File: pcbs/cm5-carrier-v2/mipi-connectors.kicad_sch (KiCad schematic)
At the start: 6 parts, among them J901 FH12-22S-0.5SH, J902 FH12-22S-0.5SH

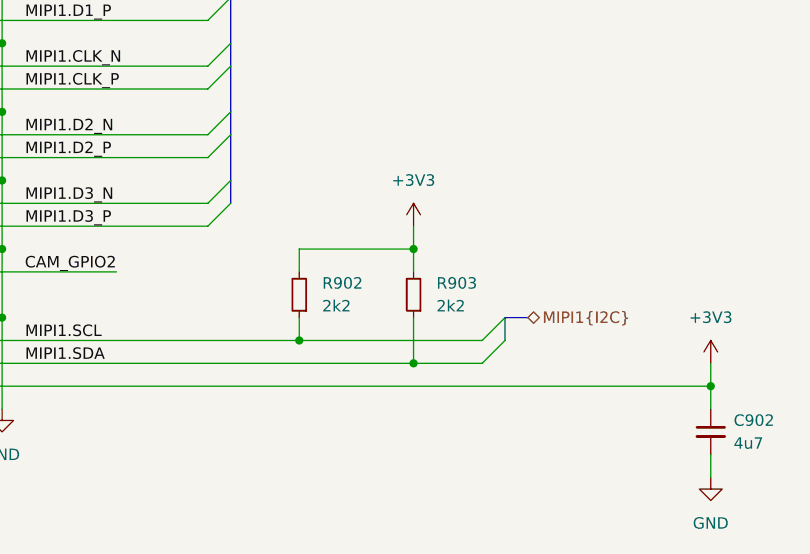
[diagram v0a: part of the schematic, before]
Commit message: Changed UART connector to I2C
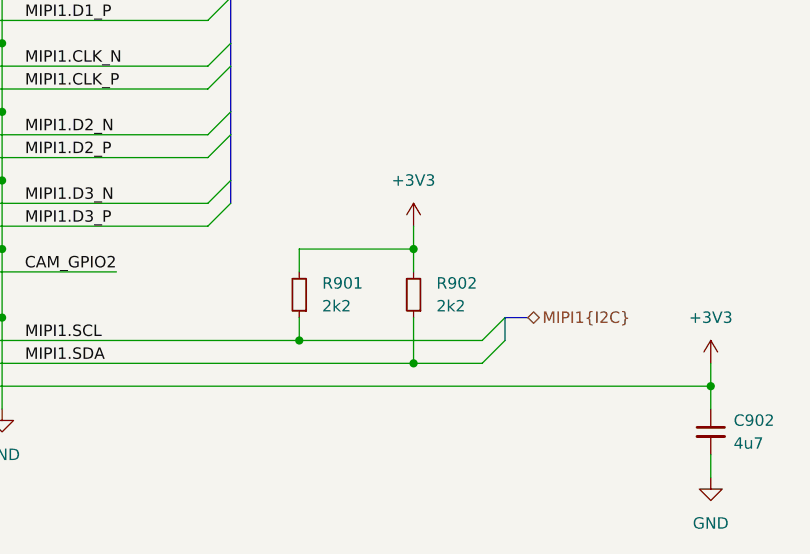
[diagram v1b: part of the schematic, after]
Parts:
- renumbered R902 to R901, R903 to R902
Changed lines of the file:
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@@
 		(dnp no)
 		(fields_autoplaced yes)
-		(property "Reference" "#PWR0902"
+		(property "Reference" "#PWR0903"
 			(at 109.22 125.73 0)
 			(hide yes)
@@
 			(project "cm5-carrier-v2"
 				(path "/f91ec272-d09a-4038-bbbb-962739a92c51/80b60915-5ccb-4842-b09a-a259b4f355b7"
-					(reference "#PWR0902")
+					(reference "#PWR0903")
 					(unit 1)
 				)
@@
 		(dnp no)
 		(fields_autoplaced yes)
-		(property "Reference" "#PWR0903"
+		(property "Reference" "#PWR0904"
 			(at 109.22 140.97 0)
 			(hide yes)
@@
 			(project "cm5-carrier-v2"
 				(path "/f91ec272-d09a-4038-bbbb-962739a92c51/80b60915-5ccb-4842-b09a-a259b4f355b7"
-					(reference "#PWR0903")
+					(reference "#PWR0904")
 					(unit 1)
 				)
@@
 		(dnp no)
 		(fields_autoplaced yes)
-		(property "Reference" "#PWR0906"
+		(property "Reference" "#PWR0908"
 			(at 251.46 125.73 0)
 			(hide yes)
@@
 			(project "cm5-carrier-v2"
 				(path "/f91ec272-d09a-4038-bbbb-962739a92c51/80b60915-5ccb-4842-b09a-a259b4f355b7"
-					(reference "#PWR0906")
+					(reference "#PWR0908")
 					(unit 1)
 				)
@@
 		(dnp no)
 		(fields_autoplaced yes)
-		(property "Reference" "#PWR0905"
+		(property "Reference" "#PWR0907"
 			(at 218.44 110.49 0)
 			(hide yes)
@@
 			(project "cm5-carrier-v2"
 				(path "/f91ec272-d09a-4038-bbbb-962739a92c51/80b60915-5ccb-4842-b09a-a259b4f355b7"
-					(reference "#PWR0905")
+					(reference "#PWR0907")
 					(unit 1)
 				)
@@
 		(dnp no)
 		(fields_autoplaced yes)
-		(property "Reference" "#PWR0901"
+		(property "Reference" "#PWR0902"
 			(at 63.5 133.35 0)
 			(hide yes)
@@
 			(project "cm5-carrier-v2"
 				(path "/f91ec272-d09a-4038-bbbb-962739a92c51/80b60915-5ccb-4842-b09a-a259b4f355b7"
-					(reference "#PWR0901")
+					(reference "#PWR0902")
 					(unit 1)
 				)
@@
 		(dnp no)
 		(fields_autoplaced yes)
-		(property "Reference" "#PWR0904"
+		(property "Reference" "#PWR0906"
 			(at 172.72 133.35 0)
 			(hide yes)
@@
 			(project "cm5-carrier-v2"
 				(path "/f91ec272-d09a-4038-bbbb-962739a92c51/80b60915-5ccb-4842-b09a-a259b4f355b7"
-					(reference "#PWR0904")
+					(reference "#PWR0906")
 					(unit 1)
 				)
@@
 		(dnp no)
 		(fields_autoplaced yes)
-		(property "Reference" "R902"
+		(property "Reference" "R901"
 			(at 208.28 113.0299 0)
 			(show_name no)
@@
 			(project "cm5-carrier-v2"
 				(path "/f91ec272-d09a-4038-bbbb-962739a92c51/80b60915-5ccb-4842-b09a-a259b4f355b7"
-					(reference "R902")
+					(reference "R901")
 					(unit 1)
 				)
@@
 		(dnp no)
 		(fields_autoplaced yes)
-		(property "Reference" "#PWR0909"
+		(property "Reference" "#PWR0901"
 			(at 38.1 133.35 0)
 			(hide yes)
@@
 			(project "cm5-carrier-v2"
 				(path "/f91ec272-d09a-4038-bbbb-962739a92c51/80b60915-5ccb-4842-b09a-a259b4f355b7"
-					(reference "#PWR0909")
+					(reference "#PWR0901")
 					(unit 1)
 				)
@@
 		(dnp no)
 		(fields_autoplaced yes)
-		(property "Reference" "#PWR0907"
+		(property "Reference" "#PWR0909"
 			(at 251.46 140.97 0)
 			(hide yes)
@@
 			(project "cm5-carrier-v2"
 				(path "/f91ec272-d09a-4038-bbbb-962739a92c51/80b60915-5ccb-4842-b09a-a259b4f355b7"
-					(reference "#PWR0907")
+					(reference "#PWR0909")
 					(unit 1)
 				)
@@
 		(dnp no)
 		(fields_autoplaced yes)
-		(property "Reference" "R903"
+		(property "Reference" "R902"
 			(at 220.98 113.0299 0)
 			(show_name no)
@@
 			(project "cm5-carrier-v2"
 				(path "/f91ec272-d09a-4038-bbbb-962739a92c51/80b60915-5ccb-4842-b09a-a259b4f355b7"
-					(reference "R903")
+					(reference "R902")
 					(unit 1)
 				)
@@
 		(dnp no)
 		(fields_autoplaced yes)
-		(property "Reference" "#PWR0908"
+		(property "Reference" "#PWR0905"
 			(at 147.32 133.35 0)
 			(hide yes)
@@
 			(project "cm5-carrier-v2"
 				(path "/f91ec272-d09a-4038-bbbb-962739a92c51/80b60915-5ccb-4842-b09a-a259b4f355b7"
-					(reference "#PWR0908")
+					(reference "#PWR0905")
 					(unit 1)
 				)
